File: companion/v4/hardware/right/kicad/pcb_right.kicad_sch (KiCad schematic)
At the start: 55 parts, among them J1 TF31-6S-0.5SH_800_, J2 speaker, J3 USB_C_Receptacle_USB2.0_14P, J4 Conn_01x24_MountingPin, SW1 SW_BOOT, SW3 SW_RESET, U2 MAX98357AETE_T, U3 USBLC6-2SC6, U4 ESP32-S3-MINI-1, U5 TLV75528PDBV, U6 TPS63001, U7 TLV75515PDBV

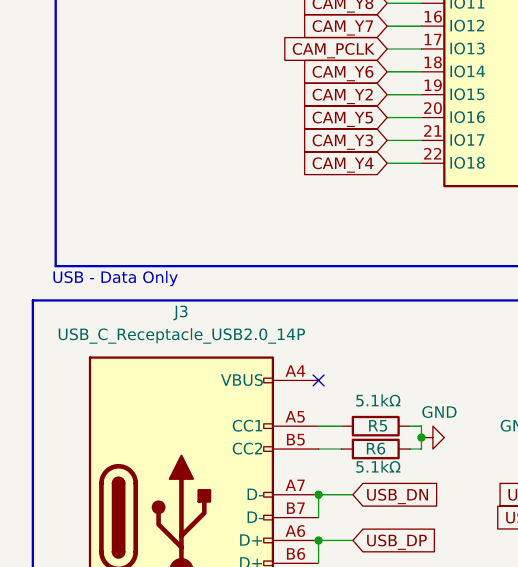
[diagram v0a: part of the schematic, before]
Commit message: addded component footprints
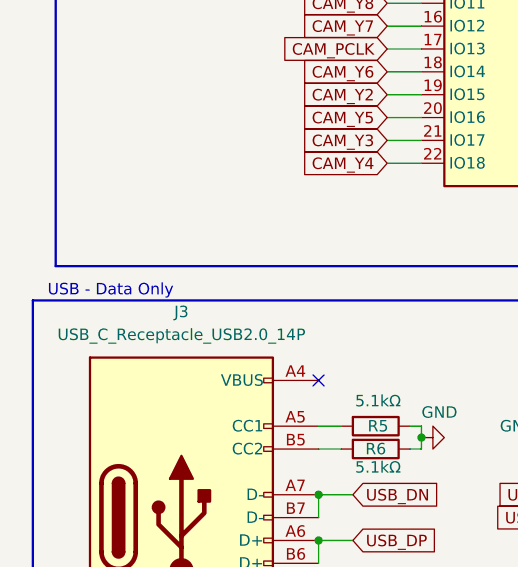
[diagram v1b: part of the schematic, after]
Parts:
- C10, C11, C12, C13, C14, C15, C16, C17, C18, C19, C20, C21, C22, C23, C24, C25, C26, C27, C28, C8, C9: footprint (none) -> Capacitor_SMD:C_0402_1005Metric
- J3: footprint (none) -> Connector_USB:USB_C_Receptacle_HRO_TYPE-C-31-M-12
- R11, R4, R5, R6: footprint (none) -> Resistor_SMD:R_0402_1005Metric
- TP2, TP3: footprint (none) -> TestPoint:TestPoint_Pad_D1.5mm
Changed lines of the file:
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@@
 	(text "USB - Data Only\n"
 		(exclude_from_sim no)
-		(at 21.844 103.124 0)
+		(at 21.336 104.394 0)
 		(effects
 			(font
@@
 			)
 		)
-		(property "Footprint" ""
+		(property "Footprint" "Resistor_SMD:R_0402_1005Metric"
 			(at 52.832 25.4 90)
 			(hide yes)
@@
 			)
 		)
-		(property "Footprint" ""
+		(property "Footprint" "Capacitor_SMD:C_0402_1005Metric"
 			(at 80.01 118.4148 0)
 			(hide yes)
@@
 			)
 		)
-		(property "Footprint" ""
+		(property "Footprint" "TestPoint:TestPoint_Pad_D1.5mm"
 			(at 100.33 35.56 0)
 			(hide yes)
@@
 			)
 		)
-		(property "Footprint" ""
+		(property "Footprint" "Capacitor_SMD:C_0402_1005Metric"
 			(at 178.7652 35.56 0)
 			(hide yes)
@@
 			)
 		)
-		(property "Footprint" ""
+		(property "Footprint" "Capacitor_SMD:C_0402_1005Metric"
 			(at 264.16 60.6552 0)
 			(hide yes)
@@
 			)
 		)
-		(property "Footprint" ""
+		(property "Footprint" "Capacitor_SMD:C_0402_1005Metric"
 			(at 94.9452 182.88 0)
 			(hide yes)
@@
 			)
 		)
-		(property "Footprint" ""
+		(property "Footprint" "Capacitor_SMD:C_0402_1005Metric"
 			(at 254.9652 88.9 0)
 			(hide yes)
@@
 			)
 		)
-		(property "Footprint" ""
+		(property "Footprint" "Resistor_SMD:R_0402_1005Metric"
 			(at 50.8 117.602 90)
 			(hide yes)
@@
 			)
 		)
-		(property "Footprint" ""
+		(property "Footprint" "Capacitor_SMD:C_0402_1005Metric"
 			(at 69.5452 27.94 0)
 			(hide yes)
@@
 			)
 		)
-		(property "Footprint" ""
+		(property "Footprint" "Capacitor_SMD:C_0402_1005Metric"
 			(at 74.6252 182.88 0)
 			(hide yes)
@@
 			)
 		)
-		(property "Footprint" ""
+		(property "Footprint" "Capacitor_SMD:C_0402_1005Metric"
 			(at 157.1752 182.88 0)
 			(hide yes)
@@
 			)
 		)
-		(property "Footprint" ""
+		(property "Footprint" "Capacitor_SMD:C_0402_1005Metric"
 			(at 240.9952 88.9 0)
 			(hide yes)
@@
 			)
 		)
-		(property "Footprint" ""
+		(property "Footprint" "Capacitor_SMD:C_0402_1005Metric"
 			(at 275.2852 88.9 0)
 			(hide yes)
@@
 			)
 		)
-		(property "Footprint" ""
+		(property "Footprint" "Capacitor_SMD:C_0402_1005Metric"
 			(at 135.5852 43.18 0)
 			(hide yes)
@@
 			)
 		)
-		(property "Footprint" ""
+		(property "Footprint" "Capacitor_SMD:C_0402_1005Metric"
 			(at 136.8552 182.88 0)
 			(hide yes)
@@
 			)
 		)
-		(property "Footprint" ""
+		(property "Footprint" "Capacitor_SMD:C_0402_1005Metric"
 			(at 260.0452 88.9 0)
 			(hide yes)
@@
 			)
 		)
-		(property "Footprint" ""
+		(property "Footprint" "Resistor_SMD:R_0402_1005Metric"
 			(at 50.8 120.142 90)
 			(hide yes)
@@
 			)
 		)
-		(property "Footprint" ""
+		(property "Footprint" "Connector_USB:USB_C_Receptacle_HRO_TYPE-C-31-M-12"
 			(at 33.02 129.54 0)
 			(hide yes)
@@
 			)
 		)
-		(property "Footprint" ""
+		(property "Footprint" "Capacitor_SMD:C_0402_1005Metric"
 			(at 183.8452 35.56 0)
 			(hide yes)
@@
 			)
 		)
-		(property "Footprint" ""
+		(property "Footprint" "Capacitor_SMD:C_0402_1005Metric"
 			(at 37.7952 52.07 0)
 			(hide yes)
@@
 			)
 		)
-		(property "Footprint" ""
+		(property "Footprint" "Capacitor_SMD:C_0402_1005Metric"
 			(at 270.2052 88.9 0)
 			(hide yes)
@@
 			)
 		)
-		(property "Footprint" ""
+		(property "Footprint" "Capacitor_SMD:C_0402_1005Metric"
 			(at 86.0552 27.94 0)
 			(hide yes)
@@
 			)
 		)
-		(property "Footprint" ""
+		(property "Footprint" "Resistor_SMD:R_0402_1005Metric"
 			(at 29.21 42.672 90)
 			(hide yes)
@@
 			)
 		)
-		(property "Footprint" ""
+		(property "Footprint" "Capacitor_SMD:C_0402_1005Metric"
 			(at 126.6952 35.56 0)
 			(hide yes)
@@
 			)
 		)
-		(property "Footprint" ""
+		(property "Footprint" "TestPoint:TestPoint_Pad_D1.5mm"
 			(at 86.36 46.99 0)
 			(hide yes)
@@
 			)
 		)
-		(property "Footprint" ""
+		(property "Footprint" "Capacitor_SMD:C_0402_1005Metric"
 			(at 46.99 40.3352 0)
 			(hide yes)
@@
 			)
 		)
-		(property "Footprint" ""
+		(property "Footprint" "Capacitor_SMD:C_0402_1005Metric"
 			(at 80.9752 27.94 0)
 			(hide yes)
@@
 			)
 		)
-		(property "Footprint" ""
+		(property "Footprint" "Capacitor_SMD:C_0402_1005Metric"
 			(at 246.0752 88.9 0)
 			(hide yes)
